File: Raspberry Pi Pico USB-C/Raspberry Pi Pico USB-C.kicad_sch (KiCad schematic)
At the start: 0 parts

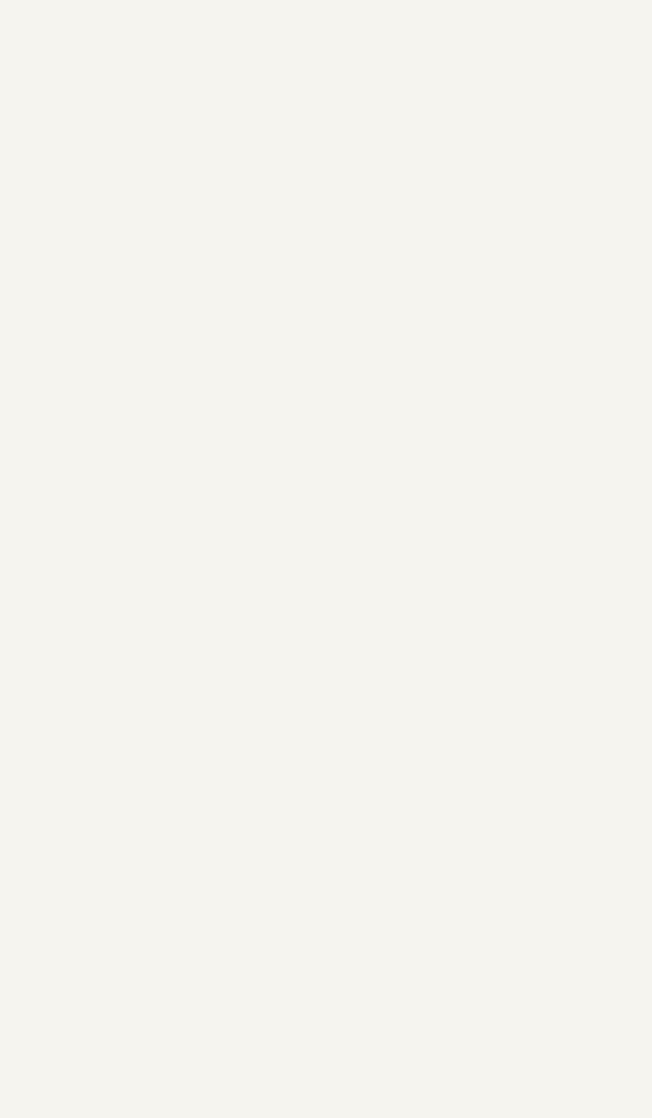
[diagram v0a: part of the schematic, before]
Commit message: Added RP2040 IC block
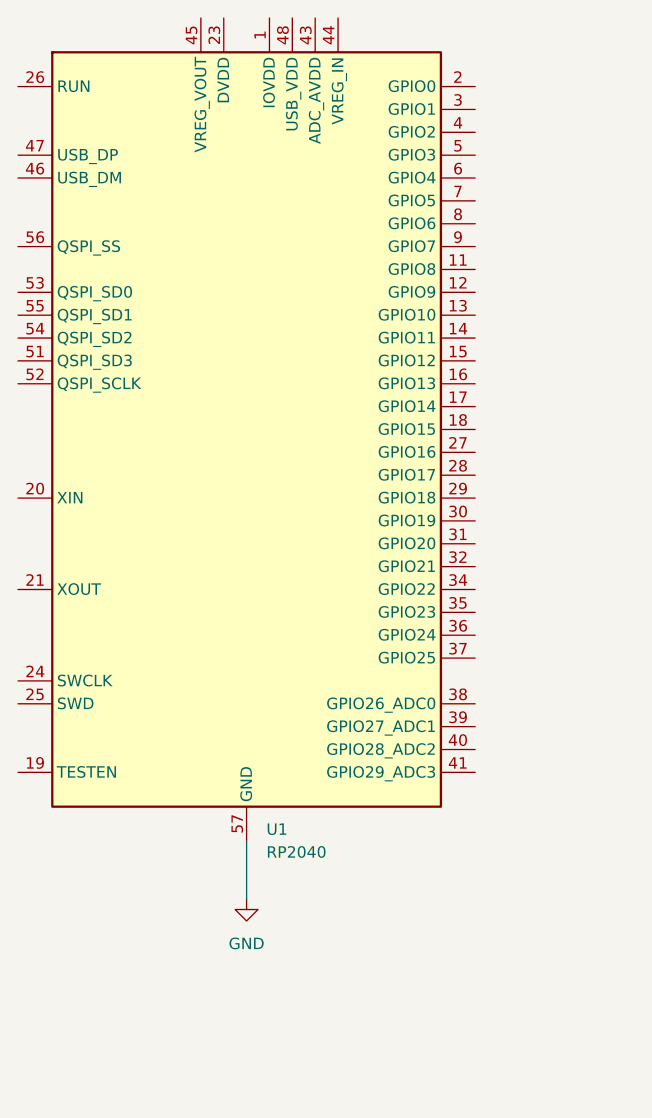
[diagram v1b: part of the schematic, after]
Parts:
- added U1: RP2040, Package_DFN_QFN:QFN-56-1EP_7x7mm_P0.4mm_EP3.2x3.2mm, symbol MCU_RaspberryPi:RP2040
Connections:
- new net: U1.1 (IOVDD), U1.10 (IOVDD), U1.22 (IOVDD), U1.33 (IOVDD), U1.42 (IOVDD), U1.49 (IOVDD)
- new net: U1.23 (DVDD), U1.50 (DVDD)
- new net GND: U1.57 (GND)
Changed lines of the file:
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@@
 (kicad_sch (version 20230121) (generator eeschema)
   (paper "A4")
+  (wire (pts (xy 97.79 125.73) (xy 97.79 132.08))
+    (stroke (width 0) (type default))
+  )
   (text "19 October 2023" (at 207.01 194.31 0)
     (effects (font (size 1.27 1.27)) (justify left bottom))
@@
     (effects (font (size 1.27 1.27)) (justify left bottom))
   )
+  (symbol (lib_id "MCU_RaspberryPi:RP2040") (at 97.79 80.01 0) (unit 1)
+    (in_bom yes) (on_board yes) (dnp no) (fields_autoplaced)
+    (property "Reference" "U1" (at 99.9841 124.46 0)
+      (effects (font (size 1.27 1.27)) (justify left))
+    )
+    (property "Value" "RP2040" (at 99.9841 127 0)
+      (effects (font (size 1.27 1.27)) (justify left))
+    )
+    (property "Footprint" "Package_DFN_QFN:QFN-56-1EP_7x7mm_P0.4mm_EP3.2x3.2mm" (at 97.79 80.01 0)
+      (effects (font (size 1.27 1.27)) hide)
+    )
+    (property "Datasheet" "https://datasheets.raspberrypi.com/rp2040/rp2040-datasheet.pdf" (at 97.79 80.01 0)
+      (effects (font (size 1.27 1.27)) hide)
+    )
+    (pin "1")
+    (pin "10")
+    (pin "11")
+    (pin "12")
+    (pin "13")
+    (pin "14")
+    (pin "15")
+    (pin "16")
+    (pin "17")
+    (pin "18")
+    (pin "19")
+    (pin "2")
+    (pin "20")
+    (pin "21")
+    (pin "22")
+    (pin "23")
+    (pin "24")
+    (pin "25")
+    (pin "26")
+    (pin "27")
+    (pin "28")
+    (pin "29")
+    (pin "3")
+    (pin "30")
+    (pin "31")
+    (pin "32")
+    (pin "33")
+    (pin "34")
+    (pin "35")
+    (pin "36")
+    (pin "37")
+    (pin "38")
+    (pin "39")
+    (pin "4")
+    (pin "40")
+    (pin "41")
+    (pin "42")
+    (pin "43")
+    (pin "44")
+    (pin "45")
+    (pin "46")
+    (pin "47")
+    (pin "48")
+    (pin "49")
+    (pin "5")
+    (pin "50")
+    (pin "51")
+    (pin "52")
+    (pin "53")
+    (pin "54")
+    (pin "55")
+    (pin "56")
+    (pin "57")
+    (pin "6")
+    (pin "7")
+    (pin "8")
+    (pin "9")
+    (instances
+      (project "Raspberry Pi Pico USB-C"
+        (path "/7f1d438c-a469-4eae-8346-8683099b0ab2"
+          (reference "U1") (unit 1)
+        )
+      )
+    )
+  )
+  (symbol (lib_id "power:GND") (at 97.79 132.08 0) (unit 1)
+    (in_bom yes) (on_board yes) (dnp no) (fields_autoplaced)
+    (property "Reference" "#PWR01" (at 97.79 138.43 0)
+      (effects (font (size 1.27 1.27)) hide)
+    )
+    (property "Value" "GND" (at 97.79 137.16 0)
+      (effects (font (size 1.27 1.27)))
+    )
+    (property "Footprint" "" (at 97.79 132.08 0)
+      (effects (font (size 1.27 1.27)) hide)
+    )
+    (property "Datasheet" "" (at 97.79 132.08 0)
+      (effects (font (size 1.27 1.27)) hide)
+    )
+    (pin "1")
+    (instances
+      (project "Raspberry Pi Pico USB-C"
+        (path "/7f1d438c-a469-4eae-8346-8683099b0ab2"
+          (reference "#PWR01") (unit 1)
+        )
+      )
+    )
+  )
   (sheet_instances

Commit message: schematic cleanup
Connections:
- net +3.3VADC: now reaches U1.43 (ADC_AVDD)
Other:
- note added: "25 July 2024"
- note removed: "19 October 2023"
- moved on the sheet: U1
